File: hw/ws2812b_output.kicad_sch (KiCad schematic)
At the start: 6 parts, among them J4 Conn_01x01, U5 SN74LVC1T45DCK

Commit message: Version 1.1 changes
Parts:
- removed TP8: TestPoint, TestPoint:TestPoint_Pad_1.0x1.0mm, symbol Connector:TestPoint
- C15: renamed from C14; value 100n -> 470n
- C16: renamed from C15; value 100n -> 470n
- J4: footprint Connector_Wire:SolderWire-0.15sqmm_1x01_D0.5mm_OD1.5mm -> Connector_Wire:SolderWire-0.5sqmm_1x01_D0.9mm_OD2.1mm; now fitted; now left out of the parts list
- R15: renamed from R13; value 33 -> 430
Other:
- note removed: "33..220 ohm right after buffer"
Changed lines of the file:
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@@
-		(color 0 0 0 0)
-	)
-	(junction
-		(at 157.48 87.63)
-		(diameter 0)
 		(color 0 0 0 0)
 	)
@@
 	(wire
 		(pts
-			(xy 153.67 87.63) (xy 157.48 87.63)
+			(xy 153.67 87.63) (xy 158.75 87.63)
 		)
 		(stroke
@@
 	(wire
 		(pts
-			(xy 157.48 87.63) (xy 158.75 87.63)
+			(xy 132.08 92.71) (xy 132.08 99.06)
 		)
 		(stroke
@@
 	(wire
 		(pts
-			(xy 132.08 92.71) (xy 132.08 99.06)
+			(xy 118.11 87.63) (xy 123.19 87.63)
 		)
 		(stroke
@@
 	(wire
 		(pts
-			(xy 118.11 87.63) (xy 123.19 87.63)
+			(xy 143.51 99.06) (xy 143.51 97.79)
 		)
 		(stroke
@@
 	(wire
 		(pts
-			(xy 157.48 86.36) (xy 157.48 87.63)
+			(xy 133.35 92.71) (xy 132.08 92.71)
 		)
 		(stroke
 			(width 0)
 			(type default)
-		)
-	)
-	(wire
-		(pts
-			(xy 143.51 99.06) (xy 143.51 97.79)
-		)
-		(stroke
-			(width 0)
-			(type default)
-		)
-	)
-	(wire
-		(pts
-			(xy 133.35 92.71) (xy 132.08 92.71)
-		)
-		(stroke
-			(width 0)
-			(type default)
-		)
-	)
-	(text "33..220 ohm right after buffer"
-		(exclude_from_sim no)
-		(at 104.14 102.87 0)
-		(effects
-			(font
-				(size 1 1)
-			)
-			(justify left bottom)
 		)
 	)
@@
 		(on_board yes)
 		(dnp no)
-		(property "Reference" "#PWR031"
+		(property "Reference" "#PWR030"
 			(at 149.86 74.93 0)
 			(effects
@@
 			(project "pxl_stick"
 				(path "/a5523c19-014c-4424-8a20-2a6215a13500/df26c79e-2c59-48fe-bad3-3c883e11f59f"
-					(reference "#PWR031")
+					(reference "#PWR030")
 					(unit 1)
 				)
@@
 		(on_board yes)
 		(dnp no)
-		(property "Reference" "C15"
+		(property "Reference" "C16"
 			(at 152.4 65.4113 0)
 			(effects
@@
 			)
 		)
-		(property "Value" "100n"
+		(property "Value" "470n"
 			(at 152.4 67.31 0)
 			(effects
@@
 			(project "pxl_stick"
 				(path "/a5523c19-014c-4424-8a20-2a6215a13500/df26c79e-2c59-48fe-bad3-3c883e11f59f"
-					(reference "C15")
+					(reference "C16")
 					(unit 1)
 				)
@@
 		(on_board yes)
 		(dnp no)
-		(property "Reference" "#PWR030"
+		(property "Reference" "#PWR029"
 			(at 137.16 74.93 0)
 			(effects
@@
 			(project "pxl_stick"
 				(path "/a5523c19-014c-4424-8a20-2a6215a13500/df26c79e-2c59-48fe-bad3-3c883e11f59f"
-					(reference "#PWR030")
+					(reference "#PWR029")
 					(unit 1)
 				)
@@
 		(mirror y)
 		(unit 1)
-		(exclude_from_sim no)
-		(in_bom yes)
-		(on_board yes)
-		(dnp yes)
+		(exclude_from_sim yes)
+		(in_bom no)
+		(on_board yes)
+		(dnp no)
 		(property "Reference" "J4"
 			(at 110.49 86.36 0)
@@
 			)
 		)
-		(property "Footprint" "Connector_Wire:SolderWire-0.15sqmm_1x01_D0.5mm_OD1.5mm"
+		(property "Footprint" "Connector_Wire:SolderWire-0.5sqmm_1x01_D0.9mm_OD2.1mm"
 			(at 113.03 87.63 0)
 			(effects
@@
 		(on_board yes)
 		(dnp no)
-		(property "Reference" "#PWR029"
+		(property "Reference" "#PWR028"
 			(at 149.86 67.31 0)
 			(effects
@@
 			(project "pxl_stick"
 				(path "/a5523c19-014c-4424-8a20-2a6215a13500/df26c79e-2c59-48fe-bad3-3c883e11f59f"
-					(reference "#PWR029")
+					(reference "#PWR028")
 					(unit 1)
 				)
@@
 		(on_board yes)
 		(dnp no)
-		(property "Reference" "#PWR032"
+		(property "Reference" "#PWR031"
 			(at 140.97 81.28 0)
 			(effects
@@
 			(project "pxl_stick"
 				(path "/a5523c19-014c-4424-8a20-2a6215a13500/df26c79e-2c59-48fe-bad3-3c883e11f59f"
-					(reference "#PWR032")
-					(unit 1)
-				)
-			)
-		)
-	)
-	(symbol
-		(lib_id "Connector:TestPoint")
-		(at 157.48 86.36 0)
-		(unit 1)
-		(exclude_from_sim no)
-		(in_bom no)
-		(on_board yes)
-		(dnp no)
-		(fields_autoplaced yes)
-		(property "Reference" "TP8"
-			(at 160.02 82.423 0)
-			(effects
-				(font
-					(size 1.27 1.27)
-				)
-				(justify left)
-			)
-		)
-		(property "Value" "TestPoint"
-			(at 160.02 84.963 0)
-			(effects
-				(font
-					(size 1.27 1.27)
-				)
-				(justify left)
-				(hide yes)
-			)
-		)
-		(property "Footprint" "TestPoint:TestPoint_Pad_1.0x1.0mm"
-			(at 162.56 86.36 0)
-			(effects
-				(font
-					(size 1.27 1.27)
-				)
-				(hide yes)
-			)
-		)
-		(property "Datasheet" "~"
-			(at 162.56 86.36 0)
-			(effects
-				(font
-					(size 1.27 1.27)
-				)
-				(hide yes)
-			)
-		)
-		(property "Description" ""
-			(at 157.48 86.36 0)
-			(effects
-				(font
-					(size 1.27 1.27)
-				)
-				(hide yes)
-			)
-		)
-		(pin "1"
-		)
-		(instances
-			(project "pxl_stick"
-				(path "/a5523c19-014c-4424-8a20-2a6215a13500/df26c79e-2c59-48fe-bad3-3c883e11f59f"
-					(reference "TP8")
+					(reference "#PWR031")
 					(unit 1)
 				)
@@
 		(on_board yes)
 		(dnp no)
-		(property "Reference" "#PWR028"
+		(property "Reference" "#PWR027"
 			(at 137.16 67.31 0)
 			(effects
@@
 			(project "pxl_stick"
 				(path "/a5523c19-014c-4424-8a20-2a6215a13500/df26c79e-2c59-48fe-bad3-3c883e11f59f"
-					(reference "#PWR028")
+					(reference "#PWR027")
 					(unit 1)
 				)
@@
 		(on_board yes)
 		(dnp no)
-		(property "Reference" "C14"
+		(property "Reference" "C15"
 			(at 139.7 65.4113 0)
 			(effects
@@
 			)
 		)
-		(property "Value" "100n"
+		(property "Value" "470n"
 			(at 139.7 67.31 0)
 			(effects
@@
 			(project "pxl_stick"
 				(path "/a5523c19-014c-4424-8a20-2a6215a13500/df26c79e-2c59-48fe-bad3-3c883e11f59f"
-					(reference "C14")
+					(reference "C15")
 					(unit 1)
 				)
@@
 		(on_board yes)
 		(dnp no)
-		(property "Reference" "R13"
+		(property "Reference" "R15"
 			(at 127 85.09 90)
 			(effects
@@
 			)
 		)
-		(property "Value" "33"
+		(property "Value" "430"
 			(at 127 90.17 90)
 			(effects
@@
 			(project "pxl_stick"
 				(path "/a5523c19-014c-4424-8a20-2a6215a13500/df26c79e-2c59-48fe-bad3-3c883e11f59f"
-					(reference "R13")
+					(reference "R15")
 					(unit 1)
 				)
@@
 		(on_board yes)
 		(dnp no)
-		(property "Reference" "#PWR034"
+		(property "Reference" "#PWR033"
 			(at 143.51 106.68 0)
 			(effects
@@
 			(project "pxl_stick"
 				(path "/a5523c19-014c-4424-8a20-2a6215a13500/df26c79e-2c59-48fe-bad3-3c883e11f59f"
-					(reference "#PWR034")
+					(reference "#PWR033")
 					(unit 1)
 				)
@@
 		(on_board yes)
 		(dnp no)
-		(property "Reference" "#PWR033"
+		(property "Reference" "#PWR032"
 			(at 146.05 81.28 0)
 			(effects
@@
 			(project "pxl_stick"
 				(path "/a5523c19-014c-4424-8a20-2a6215a13500/df26c79e-2c59-48fe-bad3-3c883e11f59f"
-					(reference "#PWR033")
-					(unit 1)
-				)
+					(reference "#PWR032")
+					(unit 1)
+				)

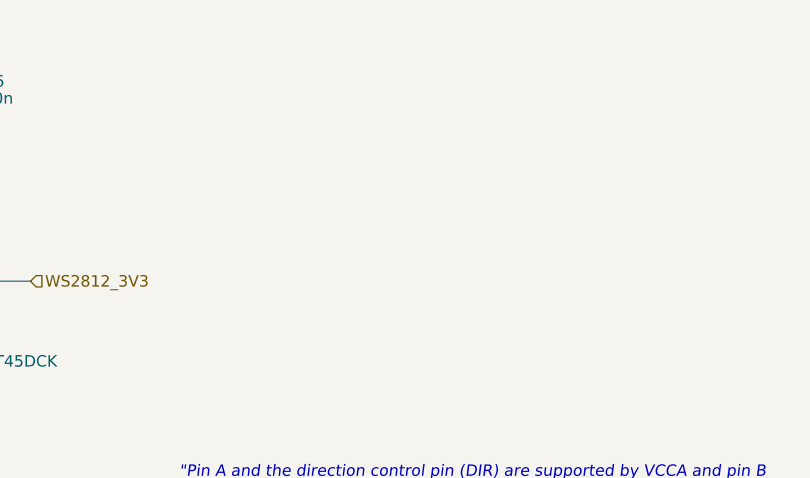
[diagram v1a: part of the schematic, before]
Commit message: Add footprint for 2 channel level shifter
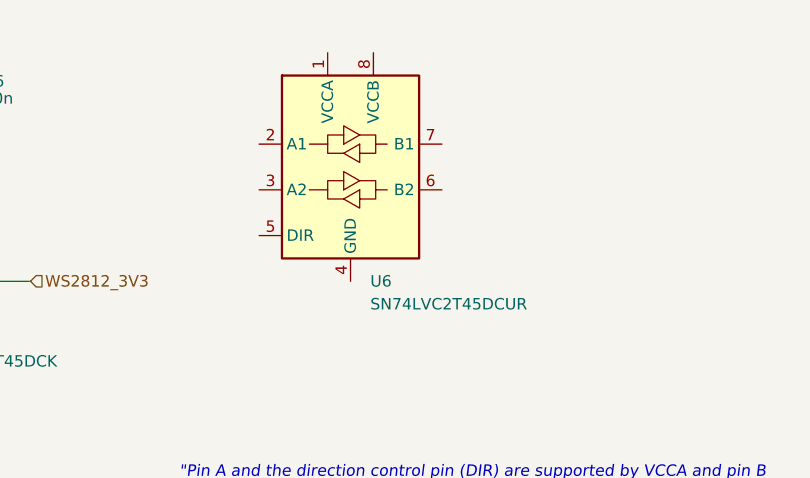
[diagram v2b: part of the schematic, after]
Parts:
- added U6: SN74LVC2T45DCUR, Package_SO:VSSOP-8_2.3x2mm_P0.5mm, symbol Logic_LevelTranslator:SN74LVC2T45DCUR
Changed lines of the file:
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@@
+	)
+	(symbol
+		(lib_id "Logic_LevelTranslator:SN74LVC2T45DCUR")
+		(at 194.31 74.93 0)
+		(unit 1)
+		(exclude_from_sim no)
+		(in_bom yes)
+		(on_board yes)
+		(dnp no)
+		(fields_autoplaced yes)
+		(property "Reference" "U6"
+			(at 196.5041 87.63 0)
+			(effects
+				(font
+					(size 1.27 1.27)
+				)
+				(justify left)
+			)
+		)
+		(property "Value" "SN74LVC2T45DCUR"
+			(at 196.5041 90.17 0)
+			(effects
+				(font
+					(size 1.27 1.27)
+				)
+				(justify left)
+			)
+		)
+		(property "Footprint" "Package_SO:VSSOP-8_2.3x2mm_P0.5mm"
+			(at 195.58 88.9 0)
+			(effects
+				(font
+					(size 1.27 1.27)
+				)
+				(hide yes)
+			)
+		)
+		(property "Datasheet" "http://www.ti.com/lit/ds/symlink/sn74lvc2t45.pdf"
+			(at 171.45 88.9 0)
+			(effects
+				(font
+					(size 1.27 1.27)
+				)
+				(hide yes)
+			)
+		)
+		(property "Description" "Dual-Bit Dual-Supply Bus Transceiver With Configurable Voltage Translation and 3-State Outputs, VSSOP-8"
+			(at 194.31 74.93 0)
+			(effects
+				(font
+					(size 1.27 1.27)
+				)
+				(hide yes)
+			)
+		)
+		(pin "3"
+		)
+		(pin "2"
+		)
+		(pin "4"
+		)
+		(pin "1"
+		)
+		(pin "6"
+		)
+		(pin "5"
+		)
+		(pin "7"
+		)
+		(pin "8"
+		)
+		(instances
+			(project ""
+				(path "/a5523c19-014c-4424-8a20-2a6215a13500/df26c79e-2c59-48fe-bad3-3c883e11f59f"
+					(reference "U6")
+					(unit 1)
+				)
+			)
+		)
 	)
 	(symbol
